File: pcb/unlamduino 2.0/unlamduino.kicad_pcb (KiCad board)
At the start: 2 copper layers, 76.2 x 105 mm, 52 parts, among them IC2 ATMEGA328-P, P3 CONN_01X08, U1 LM2576, U2 AP111733, Y2 16MHz

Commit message: Nueva placa mejor distribuida.
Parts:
- removed Arduino_Borde: Val**, huellas:arduino_borde
- removed RESET1: SW_PUSH, Buttons_Switches_ThroughHole:SW_PUSH_SMALL
- added A6: Agujero, Mounting_Holes:MountingHole_3.2mm_M3, F.Cu at (109.6, 106.7)
- added A8: Agujero, Mounting_Holes:MountingHole_3.2mm_M3, F.Cu at (86.4, 108.0)
- added G***: LOGO, LOGO, F.Cu at (54.0, 94.0)
- added RESET: SW_PUSH, Buttons_Switches_ThroughHole:SW_PUSH_SMALL, F.Cu at (33.0, 119.4)
- moved D4 31.1 mm to (53.3, 108.0), turned to 270 degrees
- moved RN3 25.4 mm to (45.7, 107.3), turned to 270 degrees
- moved A8 24.9 mm to (110.1, 100.5)
- moved R1 23.7 mm to (56.5, 118.1), turned to 270 degrees
- moved D3 21.7 mm to (48.3, 125.1), turned to 90 degrees
- moved C1 21.1 mm to (44.5, 127.0), turned to 270 degrees
- moved RH1 20.2 mm to (43.2, 114.9), turned to 90 degrees
- moved D1 19.9 mm to (48.9, 108.0), turned to 270 degrees
- moved D2 18.9 mm to (50.8, 123.2), turned to 90 degrees
- moved C4 17.3 mm to (64.1, 111.1)
- moved U2 17.3 mm to (85.7, 123.8), turned to 180 degrees
- moved C3 15.5 mm to (44.5, 119.4), turned to 270 degrees
- moved C2 14.0 mm to (55.9, 132.1), turned to 270 degrees
- moved RN1 11.7 mm to (53.3, 120.7), turned to 90 degrees
- moved C8 10.8 mm to (94.0, 101.6), turned to 180 degrees
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- renumbered PSerial1 to PuertoSerie
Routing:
- net GND: track 410.1 -> 492.6 mm
- net +5V: track 223.0 -> 277.1 mm, vias 2 -> 6
- net /TXArdu: track 107.8 -> 157.6 mm
- net /RXArdu: track 106.0 -> 152.5 mm
- net /IO13: track 147.5 -> 187.2 mm
- net /AREF: track 77.5 -> 107.6 mm
- net /VIN: track 88.9 -> 118.5 mm, vias 0 -> 2
- net /IO12: track 133.4 -> 161.7 mm
- net Net-(C1-Pad1): track 12.6 -> 39.8 mm
- net +3V3: track 24.9 -> 51.3 mm
- net /Fuente0: track 65.8 -> 89.8 mm, vias 0 -> 2
- net Net-(D4-Pad1): track 0.00 -> 13.4 mm
- net (no net): track 10.2 -> 0.00 mm
- net /IO1: track 40.9 -> 45.9 mm
- net /RESET: track 237.4 -> 233.0 mm
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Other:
- board size 76.2 x 105 mm -> 69.8 x 96.5 mm
- board text added: "->RX <-TX"
- board text added: "0 1 2 *3 4 *5 *6 7 8 *9 *10 *11 12 13 GND Aref"
- board text added: "A5 A4 A3 A2 A1 A0"
- board text added: "ANALOGICO"
- board text added: "DIGITAL (PWM*)"
- board text added: "DTR RXA TXA +5V NC GND"
- board text added: "DTR RXArdu TXArdu +5V NC GND"
- board text added: "MISO +5V SCK MOSI RST GND"
- board text added: "POWER"
- board text added: "Puerto Serie"
- board text added: "V+"
- board text added: "Vin GND GND 5V 3.3V RESET IOref NC"
- board text removed: "+5V"
- board text removed: "RXArdu"
- board text removed: "TXArdu"
- board text removed: "V"

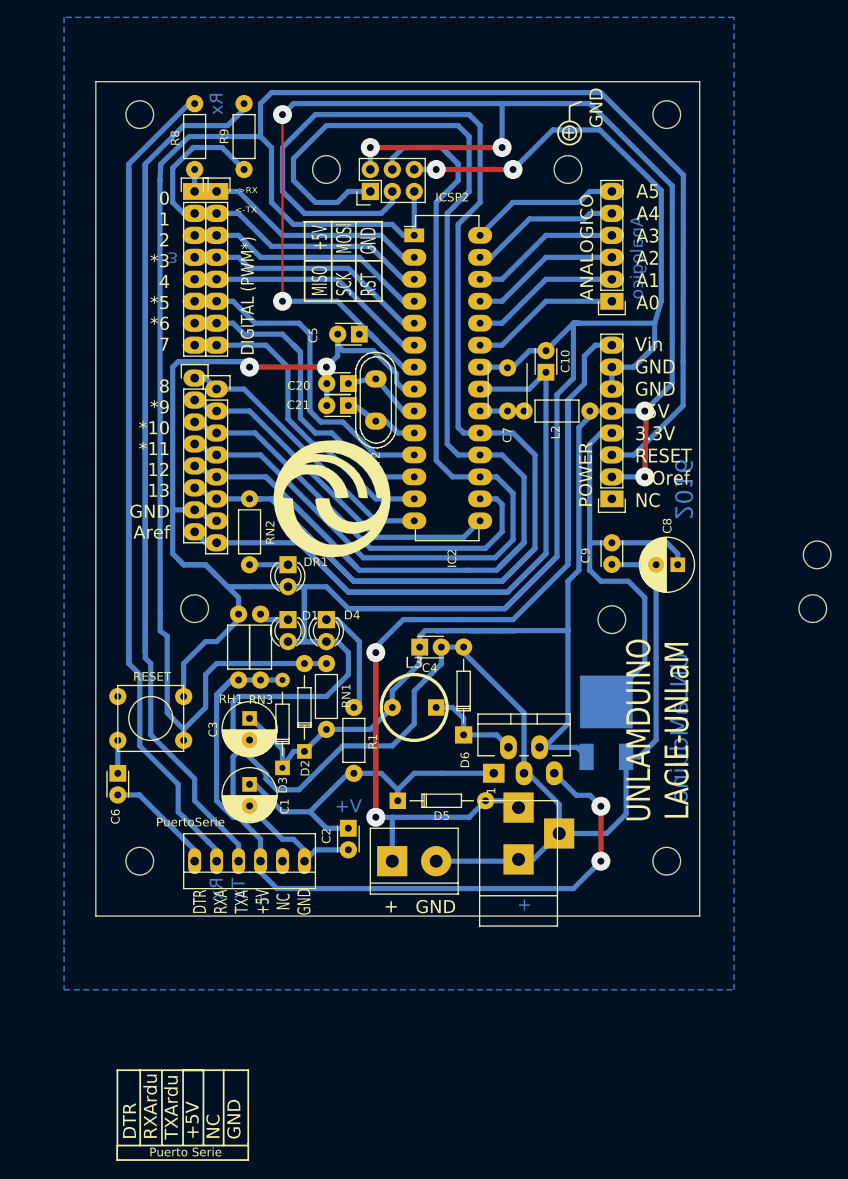
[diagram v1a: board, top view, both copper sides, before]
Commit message: Cambios minimos, limpieza de trazos redundantes y movimineto de algunas pistas para maximizar llenado.
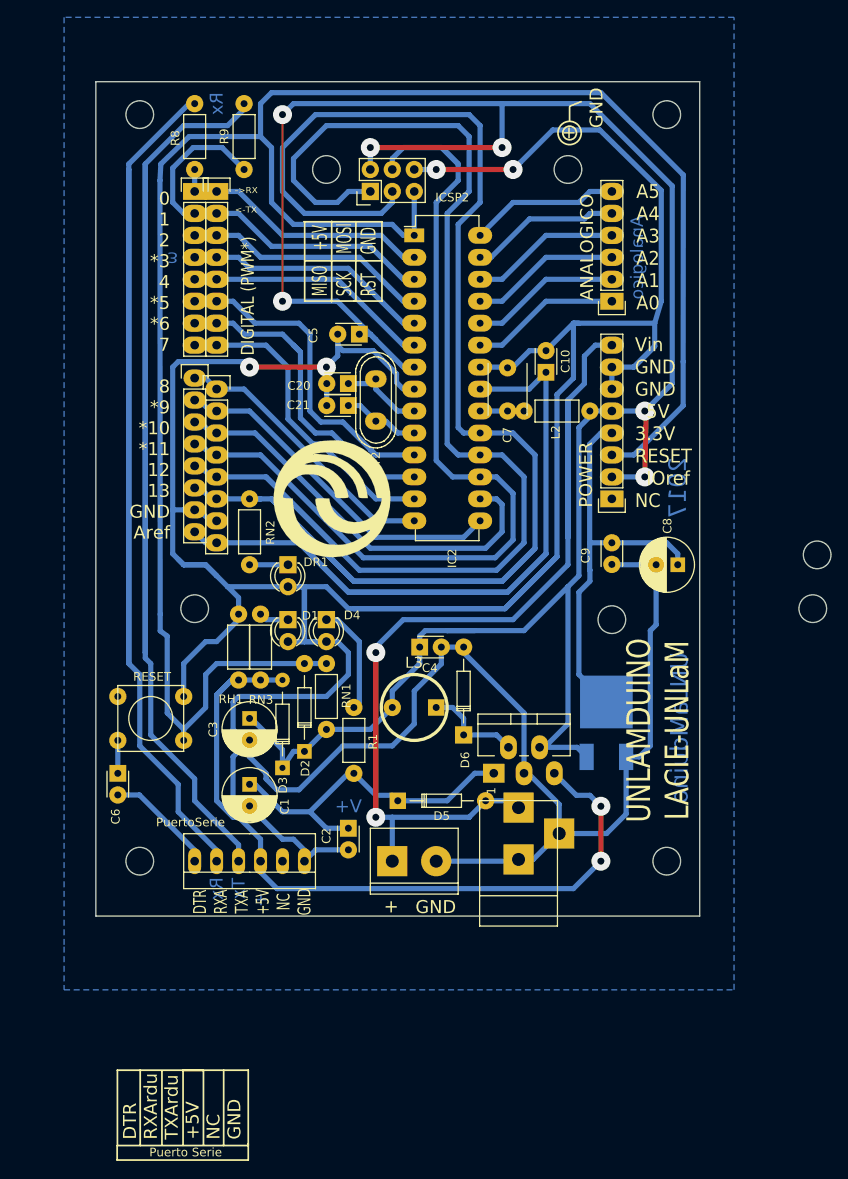
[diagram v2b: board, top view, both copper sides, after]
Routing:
- net /IO12: track 161.7 -> 149.3 mm
- net +5V: track 277.1 -> 266.6 mm
- net /VIN: track 118.5 -> 113.1 mm
- net +3V3: track 51.3 -> 46.8 mm
- net /XTAL2: track 11.9 -> 9.77 mm
- net /XTAL1: track 10.4 -> 12.5 mm
- net GND: track 492.6 -> 491.8 mm
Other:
- board text added: "2017"
- board text removed: "2016"

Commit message: Mejoras esteticas, cambio de serigrafía, alineacion de R y diodos, instrucciones en cobre.
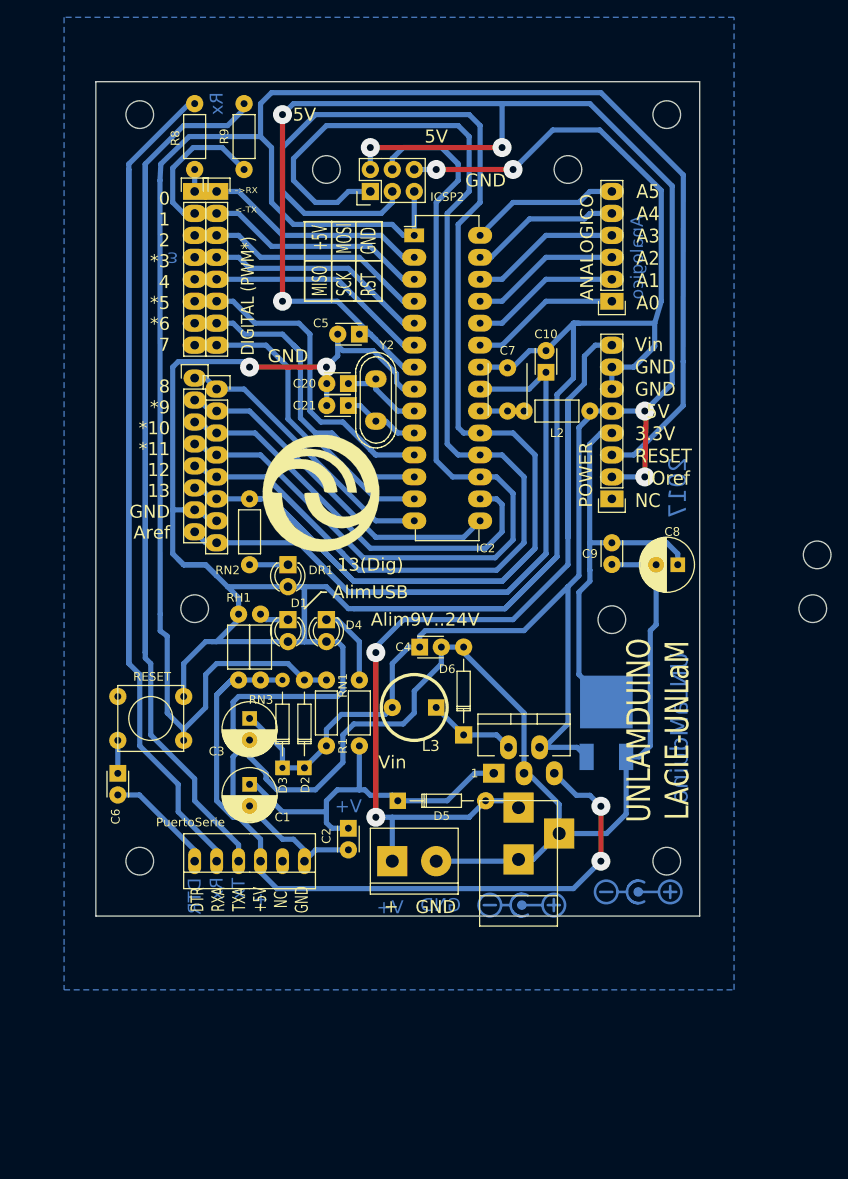
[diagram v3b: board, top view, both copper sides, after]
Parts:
- added G***: LOGO, w_logo:Logo_copper_polarity_center_10x2.8mm, B.Cu at (75.9, 141.0)
- added G***: LOGO, w_logo:Logo_copper_polarity_center_10x2.8mm, B.Cu at (89.4, 139.4)
- moved R1 3.24 mm to (57.1, 114.9)
- moved D2 1.91 mm to (50.8, 125.1)
- moved RN1 1.91 mm to (53.3, 122.6)
- moved G*** 1.42 mm to (52.7, 93.3)
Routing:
- net GND: track 491.8 -> 501.9 mm
- net Net-(C1-Pad1): track 39.6 -> 43.6 mm
- net Net-(D4-Pad1): track 13.4 -> 9.57 mm
- net +5V: track 266.6 -> 265.1 mm
- net Net-(D6-Pad1): track 11.7 -> 10.5 mm
- net /RESET: track 233.0 -> 233.8 mm
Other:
- board text added: "13(Dig)"
- board text added: "5V"
- board text added: "Alim9V..24V"
- board text added: "AlimUSB"
- board text added: "DTR"
- board text added: "Vin"
- board text removed: "DTR RXArdu TXArdu +5V NC GND"
- board text removed: "Puerto Serie"

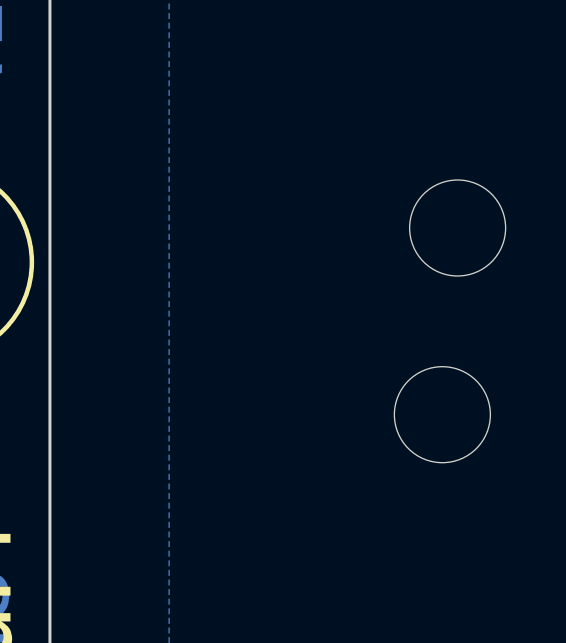
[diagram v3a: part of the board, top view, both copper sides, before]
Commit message: Correccion de agujeros de fijacion. Y en el esquematico conexion del adaptador USB-serie.
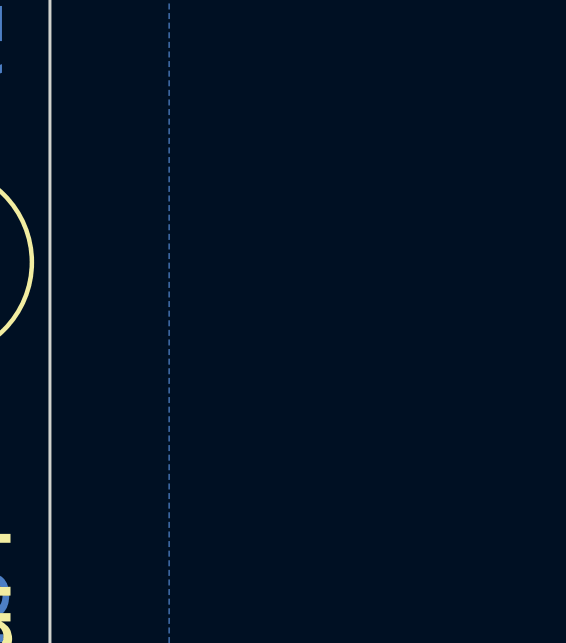
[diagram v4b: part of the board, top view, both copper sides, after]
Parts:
- removed the A6 at (38.1, 106.7)
- removed the A8 at (110.1, 100.5)
- moved A6 71.5 mm to (38.1, 106.7)
- renumbered A9 to A5
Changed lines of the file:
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@@
     (links 121)
     (no_connects 2)
-    (area 26.619999 45.669999 96.570001 142.290001)
+    (area 10.35143 37.79 115.584 157.4725)
     (thickness 1.6)
     (drawings 51)
     (tracks 601)
     (zones 0)
-    (modules 56)
+    (modules 54)
     (nets 39)
   )
@@
   )
   (setup
-    (last_trace_width 0.6)
+    (last_trace_width 0.25)
     (user_trace_width 0.6)
     (user_trace_width 0.9144)
@@
   )
   (module Mounting_Holes:MountingHole_3.2mm_M3 (layer F.Cu)
-    (at 109.601 106.68 90)
+    (at 38.1 106.68 90)
     (descr "Mounting Hole 3.2mm, no annular, M3")
     (tags "mounting hole 3.2mm no annular m3")
@@
     (descr "Mounting Hole 3.2mm, no annular, M3")
     (tags "mounting hole 3.2mm no annular m3")
-    (fp_text reference A9 (at 0 -3.175 90) (layer F.SilkS) hide
+    (fp_text reference A5 (at 0 -3.175 90) (layer F.SilkS) hide
       (effects (font (size 1 1) (thickness 0.15)))
     )
     (fp_text value Agujero (at 3.175 2.54 90) (layer F.Fab)
-      (effects (font (size 1 1) (thickness 0.15)))
-    )
-    (fp_circle (center 0 0) (end 3.2 0) (layer Cmts.User) (width 0.15))
-    (fp_circle (center 0 0) (end 3.45 0) (layer F.CrtYd) (width 0.05))
-    (pad 1 np_thru_hole circle (at 0 0 90) (size 3.2 3.2) (drill 3.2) (layers *.Cu *.Mask F.SilkS))
-  )
-  (module Mounting_Holes:MountingHole_3.2mm_M3 (layer F.Cu)
-    (at 110.109 100.457 90)
-    (descr "Mounting Hole 3.2mm, no annular, M3")
-    (tags "mounting hole 3.2mm no annular m3")
-    (fp_text reference A8 (at 0 -3.175 90) (layer F.SilkS) hide
-      (effects (font (size 1 1) (thickness 0.15)))
-    )
-    (fp_text value Agujero (at 0 4.2 90) (layer F.Fab)
       (effects (font (size 1 1) (thickness 0.15)))
     )
@@
     )
     (fp_text value Agujero (at 6.35 0 90) (layer F.Fab)
-      (effects (font (size 1 1) (thickness 0.15)))
-    )
-    (fp_circle (center 0 0) (end 3.2 0) (layer Cmts.User) (width 0.15))
-    (fp_circle (center 0 0) (end 3.45 0) (layer F.CrtYd) (width 0.05))
-    (pad 1 np_thru_hole circle (at 0 0 90) (size 3.2 3.2) (drill 3.2) (layers *.Cu *.Mask F.SilkS))
-  )
-  (module Mounting_Holes:MountingHole_3.2mm_M3 (layer F.Cu)
-    (at 38.1 106.68 90)
-    (descr "Mounting Hole 3.2mm, no annular, M3")
-    (tags "mounting hole 3.2mm no annular m3")
-    (fp_text reference A6 (at -0.635 -2.54 90) (layer F.SilkS) hide
-      (effects (font (size 1 1) (thickness 0.15)))
-    )
-    (fp_text value Agujero (at 0 2.54 90) (layer F.Fab)
       (effects (font (size 1 1) (thickness 0.15)))
     )
@@
   (segment (start 61.59298 128.905) (end 61.59552 128.90246) (width 0.6) (layer B.Cu) (net 8) (status 30))
   (segment (start 72.68972 125.73) (end 72.69988 125.71984) (width 0.6) (layer B.Cu) (net 8) (status 30))
-  (segment (start 53.34 122.555) (end 53.34 120.65) (width 0.6) (layer B.Cu) (net 9))
-  (segment (start 60.155002 118.914998) (end 60.96 118.11) (width 0.6) (layer B.Cu) (net 9))
+  (segment (start 53.34 122.555) (end 53.34 120.65) (width 0.6) (layer B.Cu) (net 9) (status 10))
+  (segment (start 60.155002 118.914998) (end 60.96 118.11) (width 0.6) (layer B.Cu) (net 9) (status 20))
   (segment (start 55.075002 118.914998) (end 60.155002 118.914998) (width 0.6) (layer B.Cu) (net 9))
   (segment (start 53.34 120.65) (end 55.075002 118.914998) (width 0.6) (layer B.Cu) (net 9))

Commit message: Conector de programacion completo.
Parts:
- removed the G*** at (75.9, 141.0)
- moved L3 5.75 mm to (64.1, 123.8)
- moved C2 3.59 mm to (53.3, 129.5), turned to 90 degrees
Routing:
- net GND: track 501.9 -> 483.2 mm
- net +3V3: track 46.8 -> 58.8 mm
- net +5V: track 265.1 -> 268.5 mm
- net Net-(C1-Pad1): track 43.6 -> 40.9 mm
- net /RXArdu: track 152.5 -> 153.8 mm
- net Net-(D6-Pad1): track 10.5 -> 9.64 mm
- net /Fuente0: track 89.8 -> 90.5 mm

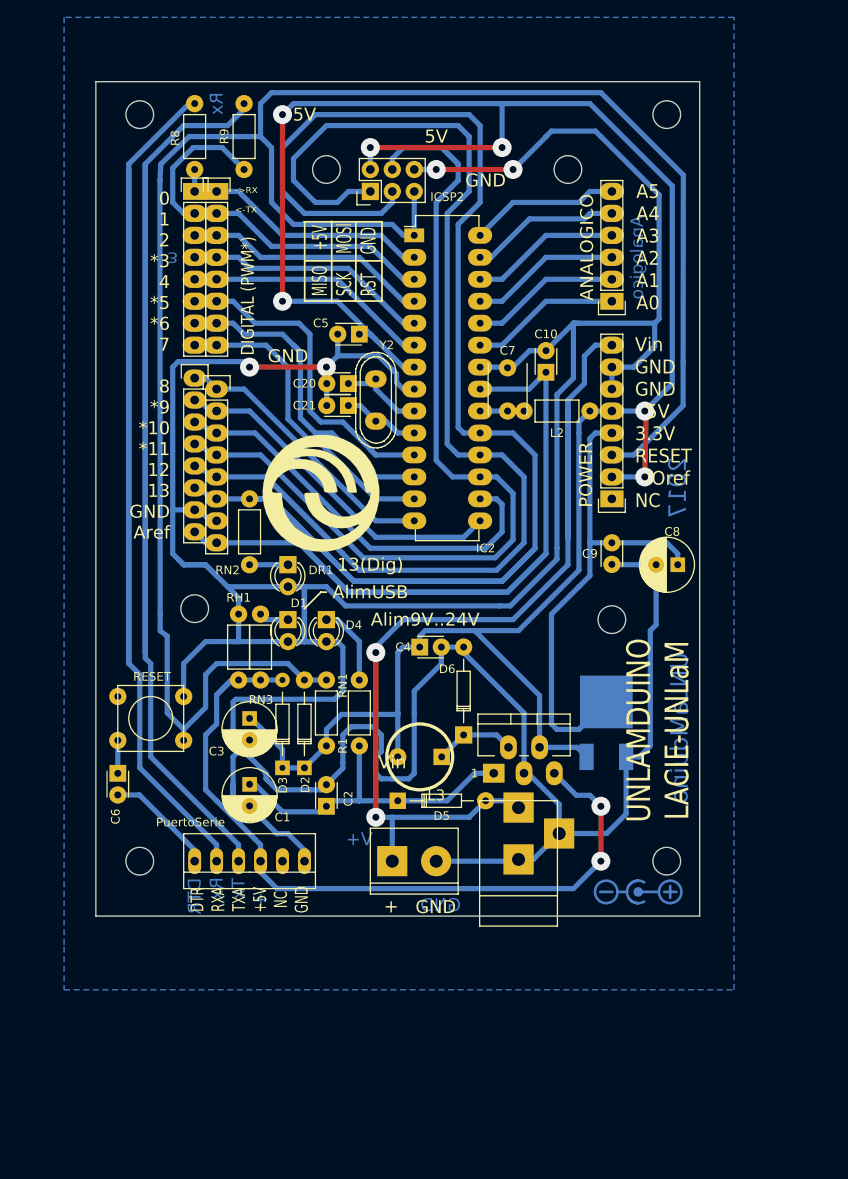
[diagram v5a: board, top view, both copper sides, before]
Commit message: Controlador puente H con ejemplo y cambios menores en pistas (limpieza de pista huérfanas).
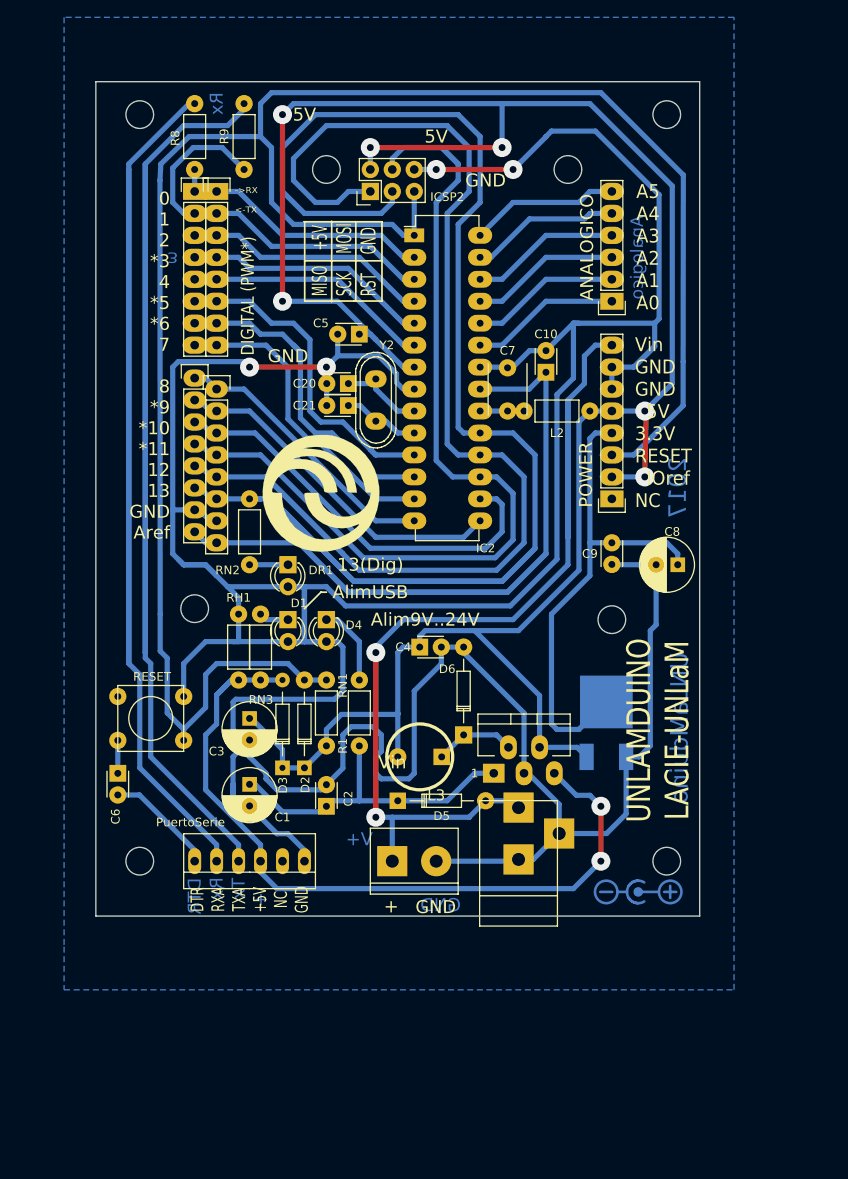
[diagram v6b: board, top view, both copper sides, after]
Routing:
- net Net-(C1-Pad1): track 40.9 -> 40.0 mm
- net /IO13: track 187.2 -> 186.4 mm
- net /IO12: track 149.3 -> 148.5 mm
